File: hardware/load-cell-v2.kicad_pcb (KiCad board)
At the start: 2 copper layers, 30 x 30 mm, 36 parts, among them P1 CON-SENSOR, P2 Boot, P3 Debug, P4 AKL_5_2, P5 AKL_5_2, U1 XMC1100, U2 FAN4860, U3 HX711, U4 DRILL, U5 DRILL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

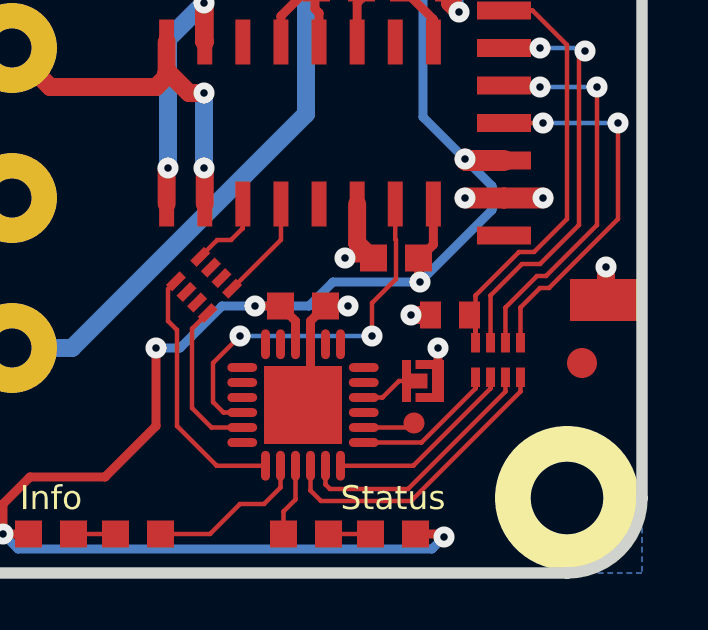
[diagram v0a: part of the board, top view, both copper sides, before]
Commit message: Change capacitor footprint(s) to C0402F
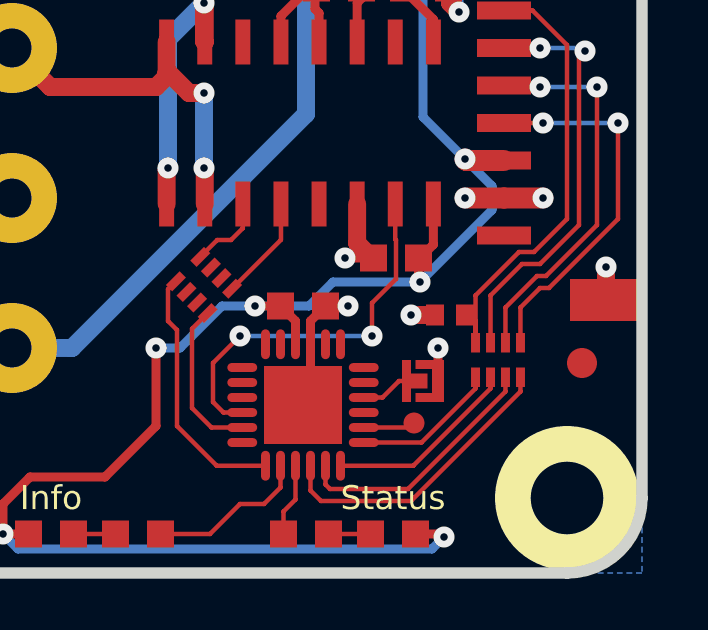
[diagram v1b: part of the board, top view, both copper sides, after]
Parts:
- C1: footprint C0402E -> kicad-libraries:C0402F
- C2, C3, C4, C5, C6, C7, C8, C9: footprint C0603F -> kicad-libraries:C0603F
- D1, D2: footprint D0603F -> kicad-libraries:D0603F
- R1, R2: footprint R0603F -> kicad-libraries:R0603F
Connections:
- P1 pad 1: (no net) -> Net-(P1-Pad1)
- RP2 pad 2: (no net) -> Net-(RP2-Pad2)
- RP2 pad 3: (no net) -> Net-(RP2-Pad3)
- RP2 pad 6: (no net) -> Net-(RP2-Pad6)
- RP2 pad 7: (no net) -> Net-(RP2-Pad7)
- U1 pad 11: (no net) -> Net-(U1-Pad11)
- U1 pad 12: (no net) -> Net-(U1-Pad12)
- U1 pad 13: (no net) -> Net-(U1-Pad13)
- U1 pad 14: (no net) -> Net-(U1-Pad14)
- U1 pad 15: (no net) -> Net-(U1-Pad15)
- U1 pad 18: (no net) -> Net-(U1-Pad18)
- U1 pad 3: (no net) -> Net-(U1-Pad3)
- U1 pad 5: (no net) -> Net-(U1-Pad5)
- U1 pad 6: (no net) -> Net-(U1-Pad6)
- U1 pad 7: (no net) -> Net-(U1-Pad7)
- U1 pad 8: (no net) -> Net-(U1-Pad8)
- U3 pad 13: (no net) -> Net-(U3-Pad13)
- U3 pad 2: (no net) -> Net-(U3-Pad2)
- U3 pad 6: (no net) -> Net-(U3-Pad6)
